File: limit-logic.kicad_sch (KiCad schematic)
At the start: 6 parts, among them U17001 4043, U17002 4043, U17003 4078

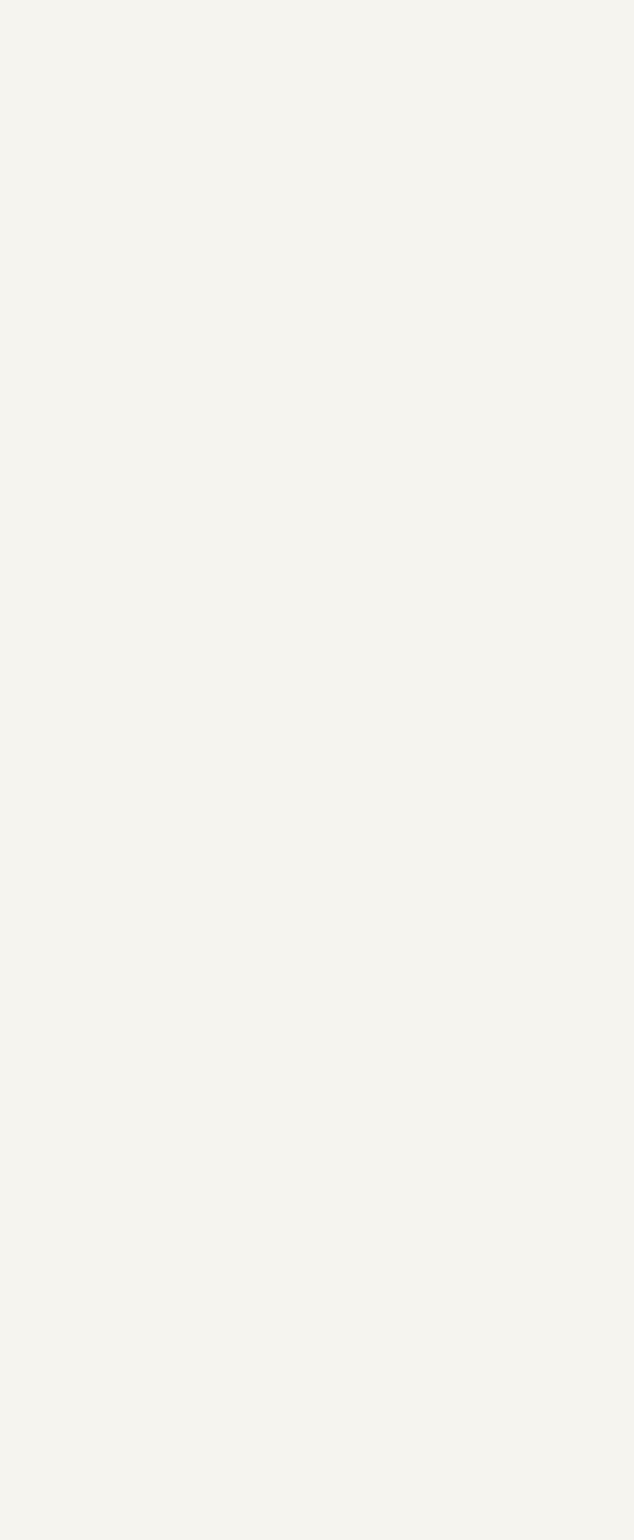
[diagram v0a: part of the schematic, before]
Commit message: add limit-logic 4081 2 input nand gate
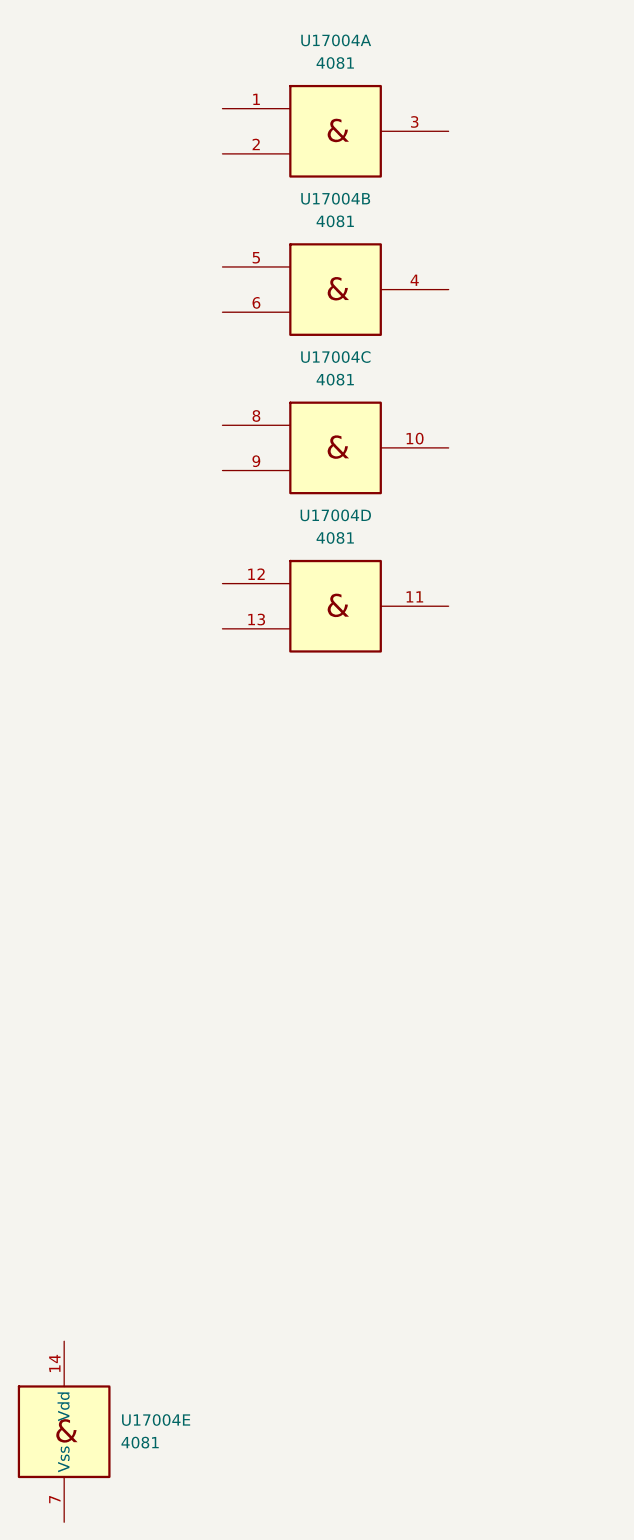
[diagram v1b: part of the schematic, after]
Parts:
- added U17004: 4081, Package_SO:SOIC-14_3.9x8.7mm_P1.27mm, symbol pss:4081

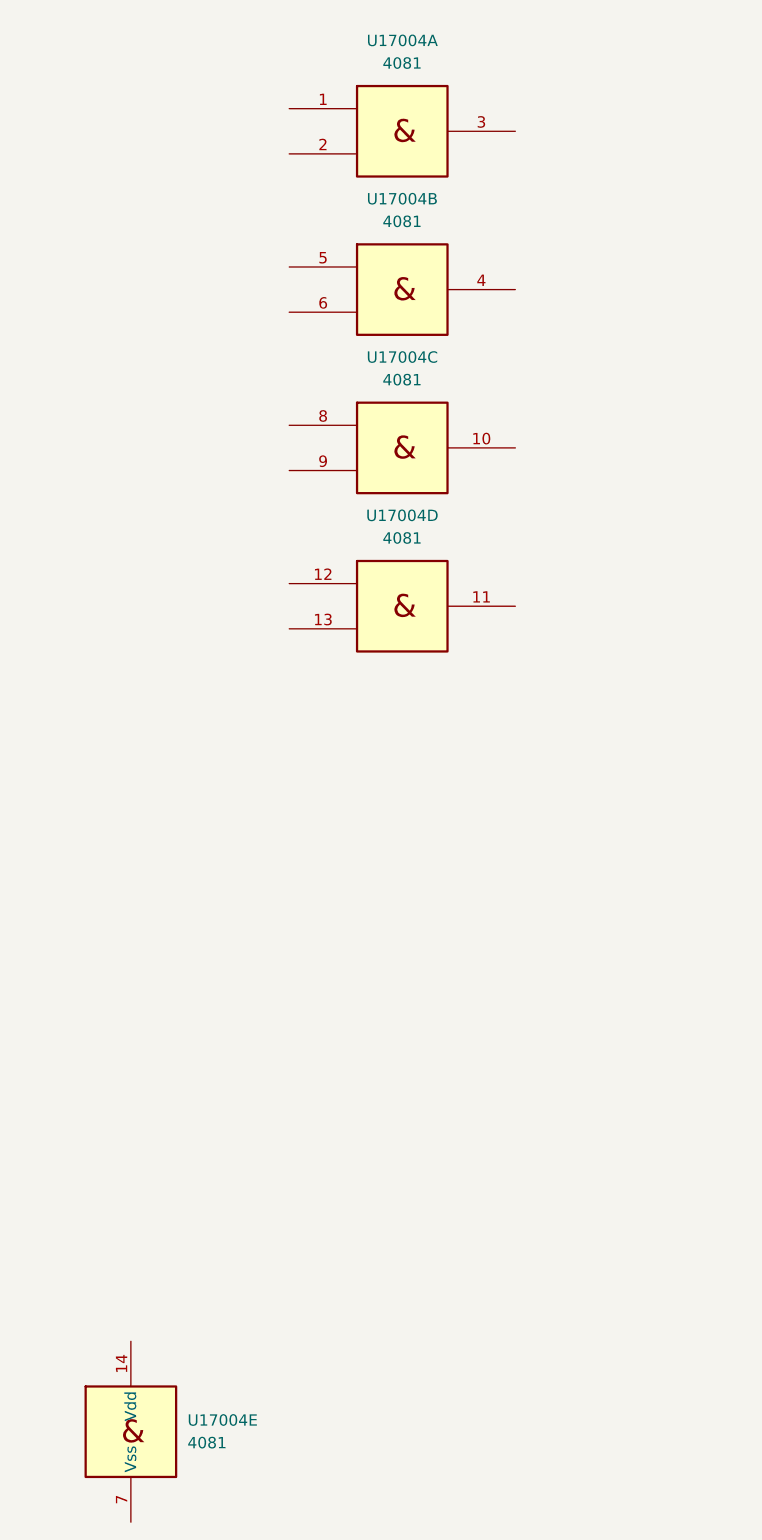
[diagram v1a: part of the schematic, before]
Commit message: add limit-logic 4073 3 input nand gate
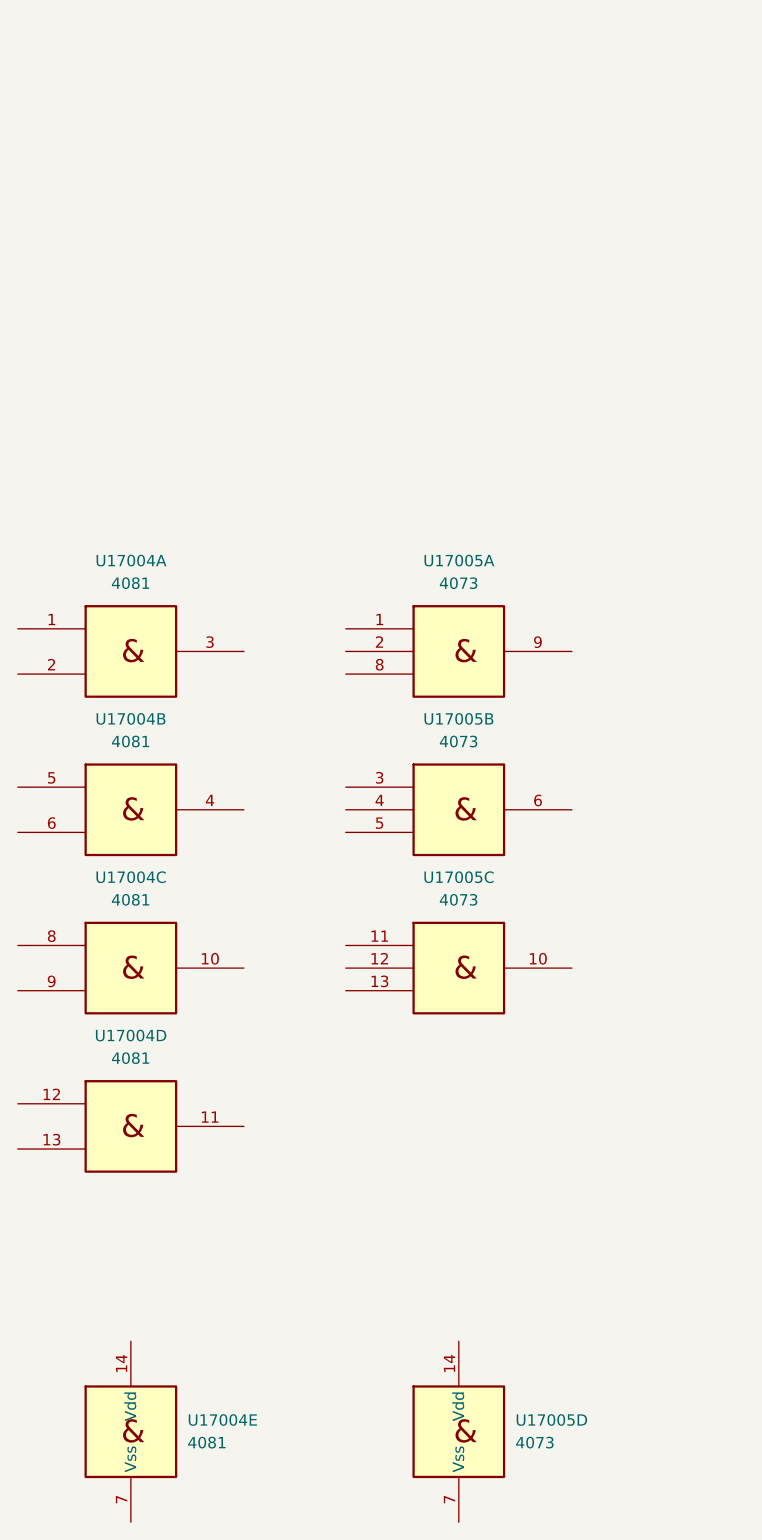
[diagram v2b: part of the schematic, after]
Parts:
- added U17005: 4073, Package_SO:SOIC-14_3.9x8.7mm_P1.27mm, symbol pss:4073
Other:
- moved on the sheet: U17004A, U17004B, U17004C, U17004D

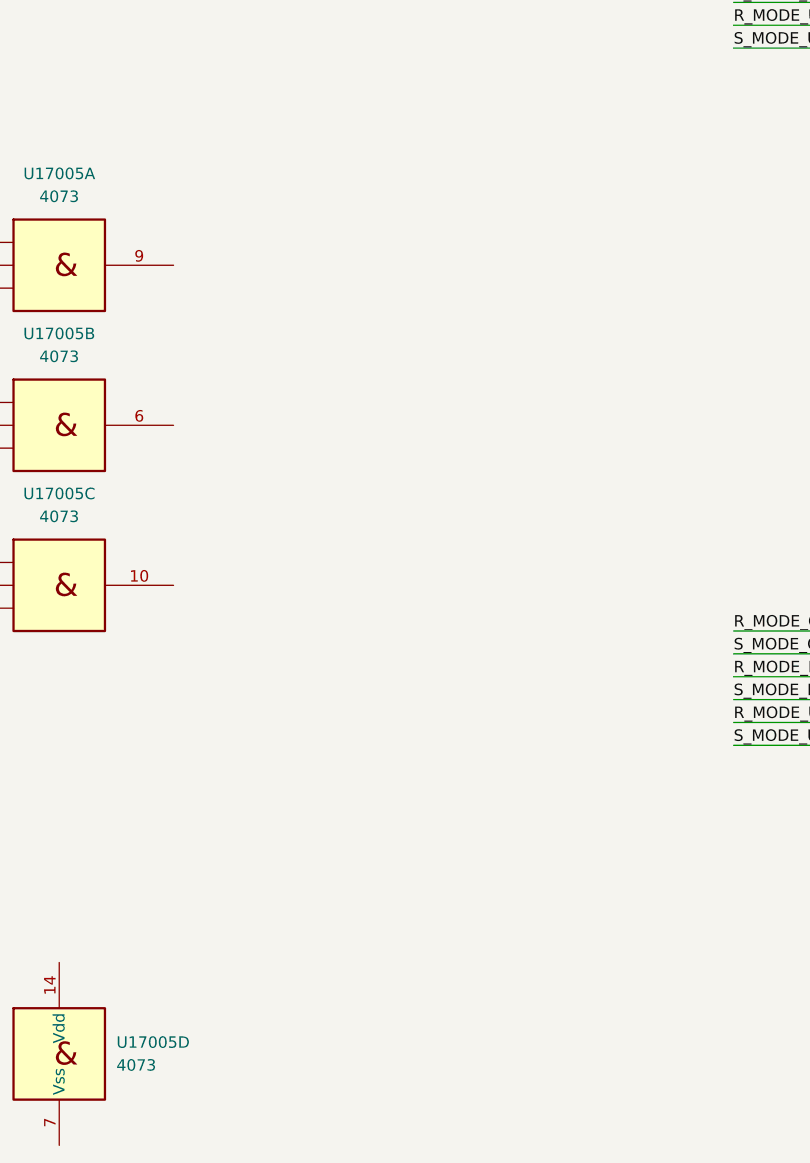
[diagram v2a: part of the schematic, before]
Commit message: add limit-logic 4071 2 input or gate
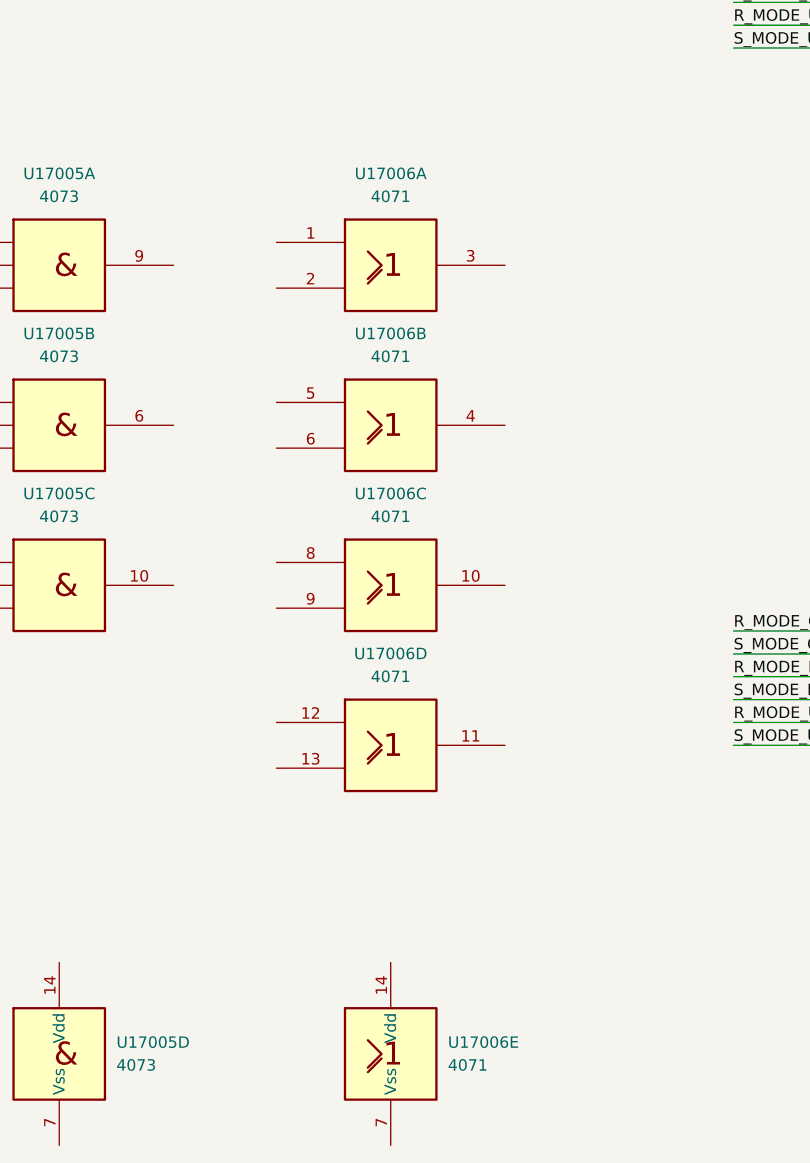
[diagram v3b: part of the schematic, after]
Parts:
- added U17006: 4071, Package_SO:SOIC-14_3.9x8.7mm_P1.27mm, symbol pss:4071

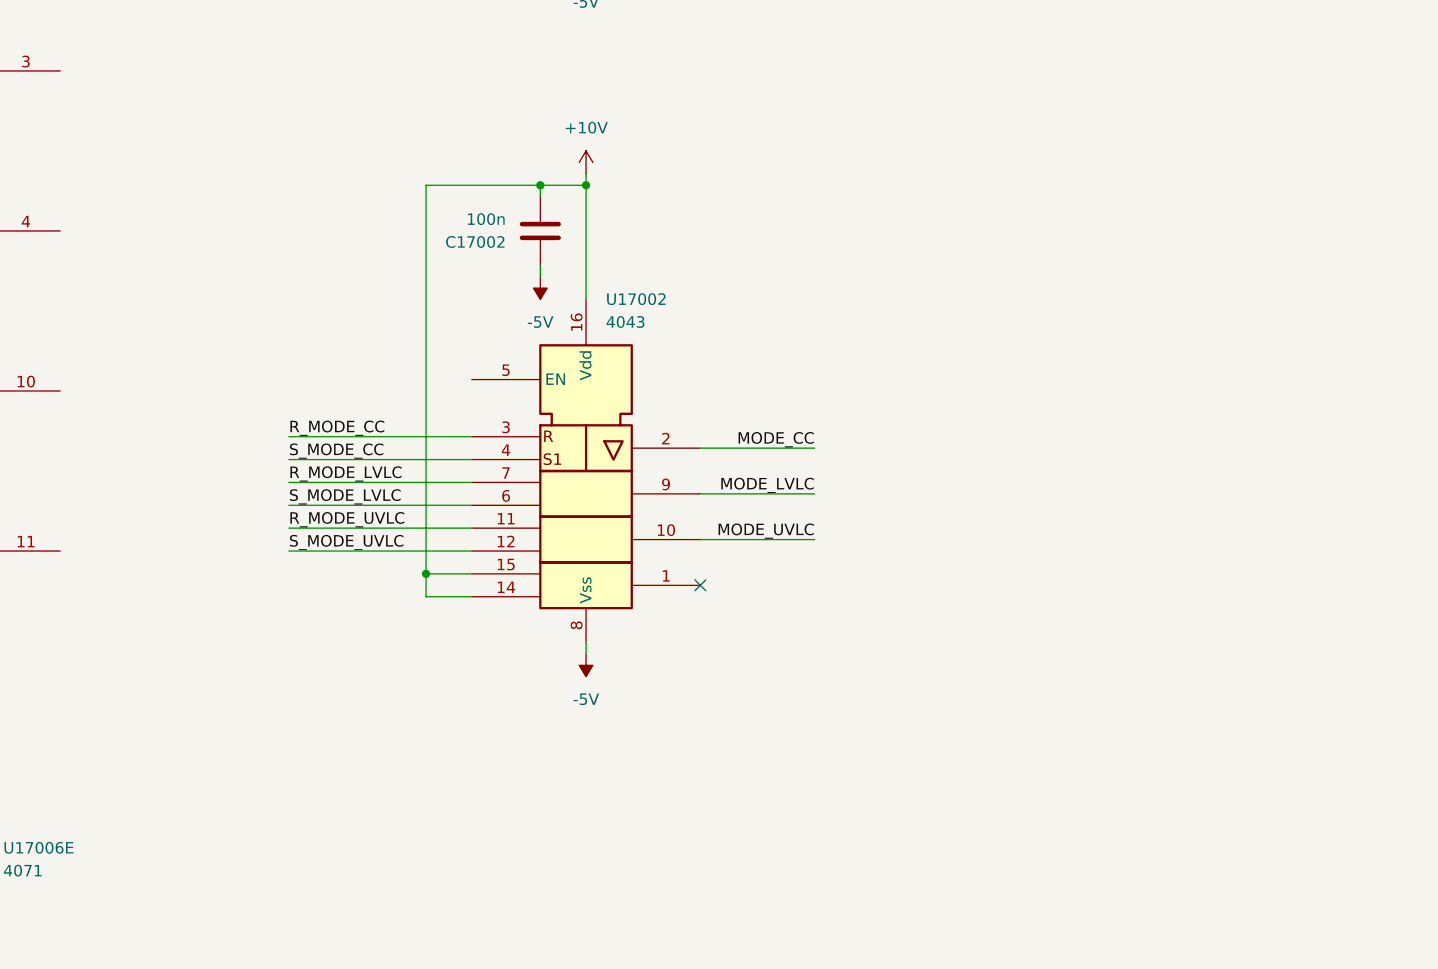
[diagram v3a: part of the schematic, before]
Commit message: add limit-logic 4069 hex inverter
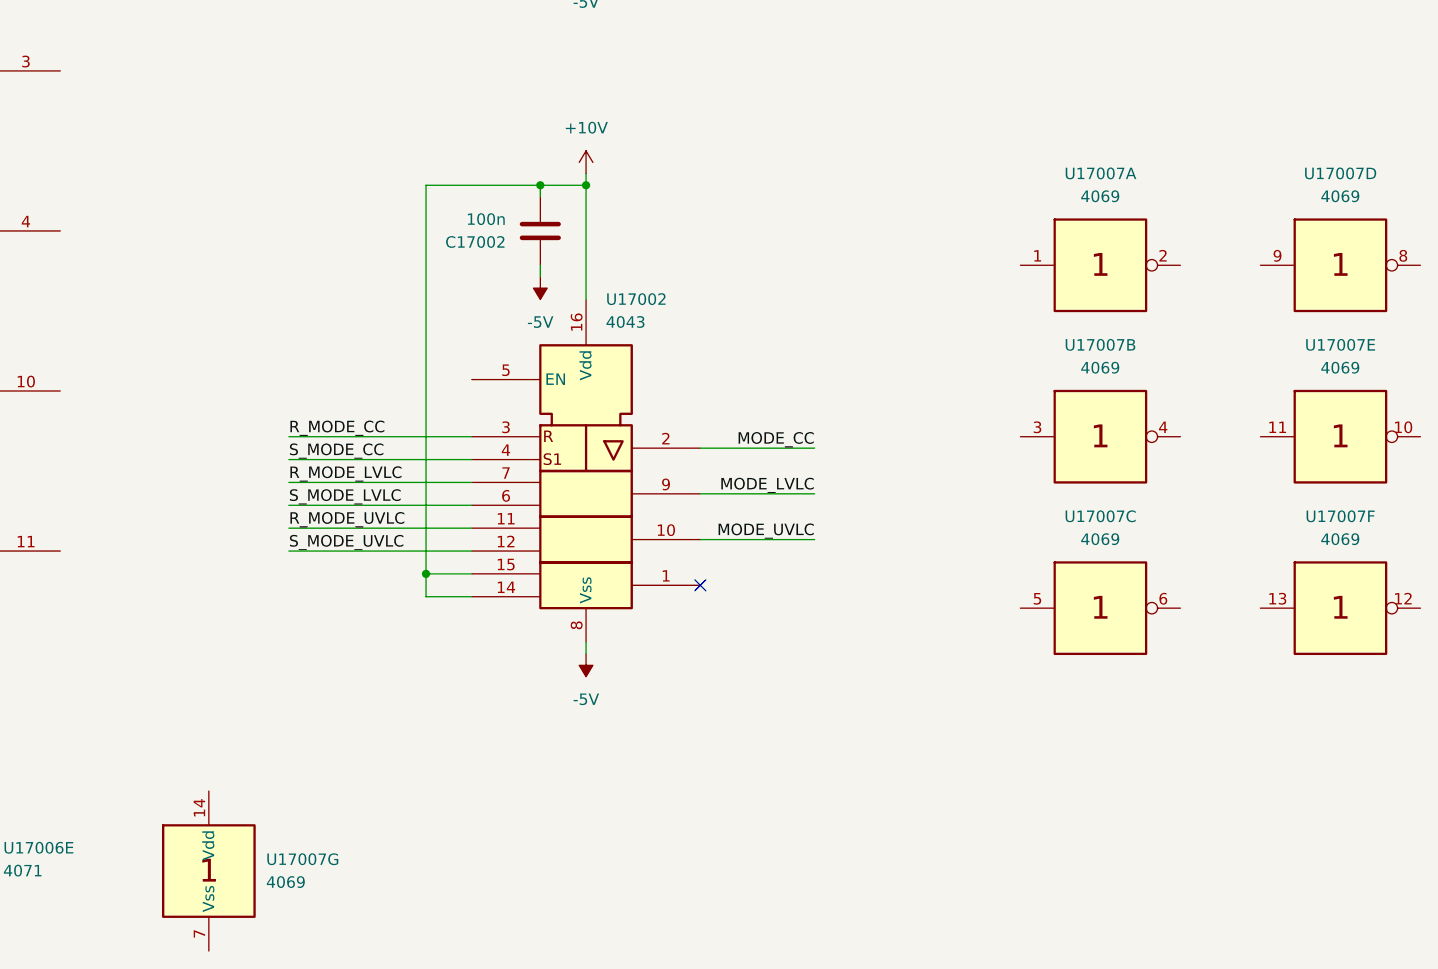
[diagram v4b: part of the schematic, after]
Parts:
- added U17007: 4069, Package_SO:SOIC-14_3.9x8.7mm_P1.27mm, symbol pss:4069
